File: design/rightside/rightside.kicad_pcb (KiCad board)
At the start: 4 copper layers, 142.6 x 96.2 mm, 227 parts, among them IC2 XC9148G50CER-G, IC3 nRF52833-QDAA-R7, IC4 74AHCT125PW,118, IC5 MCP23018T-E_SS, IC6 XC9291B33D1R-G, J1 USB_C_Receptacle_USB2.0_16P, J2 Battery Pos, J3 Battery Neg, J4 OLED_128x32, J6 Conn_01x04, J7 F32Q-1A7H1-11012, U1 BQ27441-G1, U2 BQ24072RGT, U3 USB6B1, U5 PEC11L-4015F-S0015, U6 PEC11L-4015F-S0015, Y1 ECS-320-8-37B2-JTY-TR

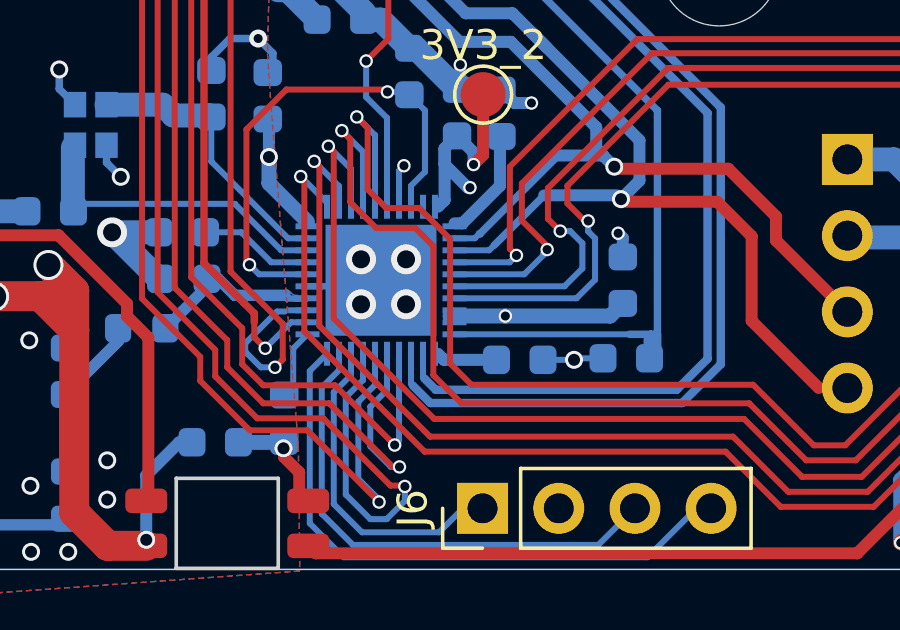
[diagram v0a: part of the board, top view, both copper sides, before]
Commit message: begin routing leftside
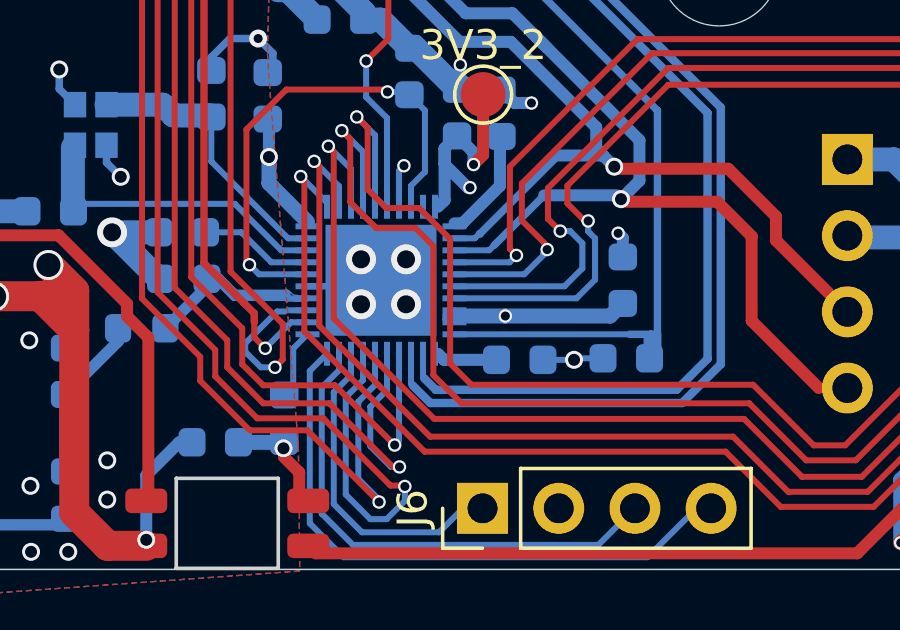
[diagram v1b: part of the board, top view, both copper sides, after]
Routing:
- net 3V3: track 84.2 -> 85.0 mm
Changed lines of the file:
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@@
+	)
+	(segment
+		(start 263.835969 166.079719)
+		(end 263.822288 166.0934)
+		(width 0.2)
+		(layer "B.Cu")
+		(net 2)
 	)
 	(segment
@@
 	)
 	(segment
+		(start 263.822288 166.0934)
+		(end 263.5505 166.0934)
+		(width 0.2)
+		(layer "B.Cu")
+		(net 2)
+	)
+	(segment
 		(start 253.410969 129.355719)
 		(end 251.885969 129.355719)
@@
 	)
 	(segment
+		(start 263.5505 166.0934)
+		(end 263.535969 166.078869)
+		(width 0.2)
+		(layer "B.Cu")
+		(net 2)
+	)
+	(segment
 		(start 276.990969 163.350719)
 		(end 276.930969 163.290719)
@@
 	)
 	(segment
+		(start 263.535969 166.078869)
+		(end 263.535969 165.8934)
+		(width 0.2)
+		(layer "B.Cu")
+		(net 2)
+	)
+	(segment
 		(start 263.505969 160.380719)
 		(end 263.505969 162.109719)
@@
 		(layer "B.Cu")
 		(net 2)
+	)
+	(segment
+		(start 263.835969 165.779719)
+		(end 263.835969 166.079719)
+		(width 0.2)
+		(layer "B.Cu")
+		(net 2)

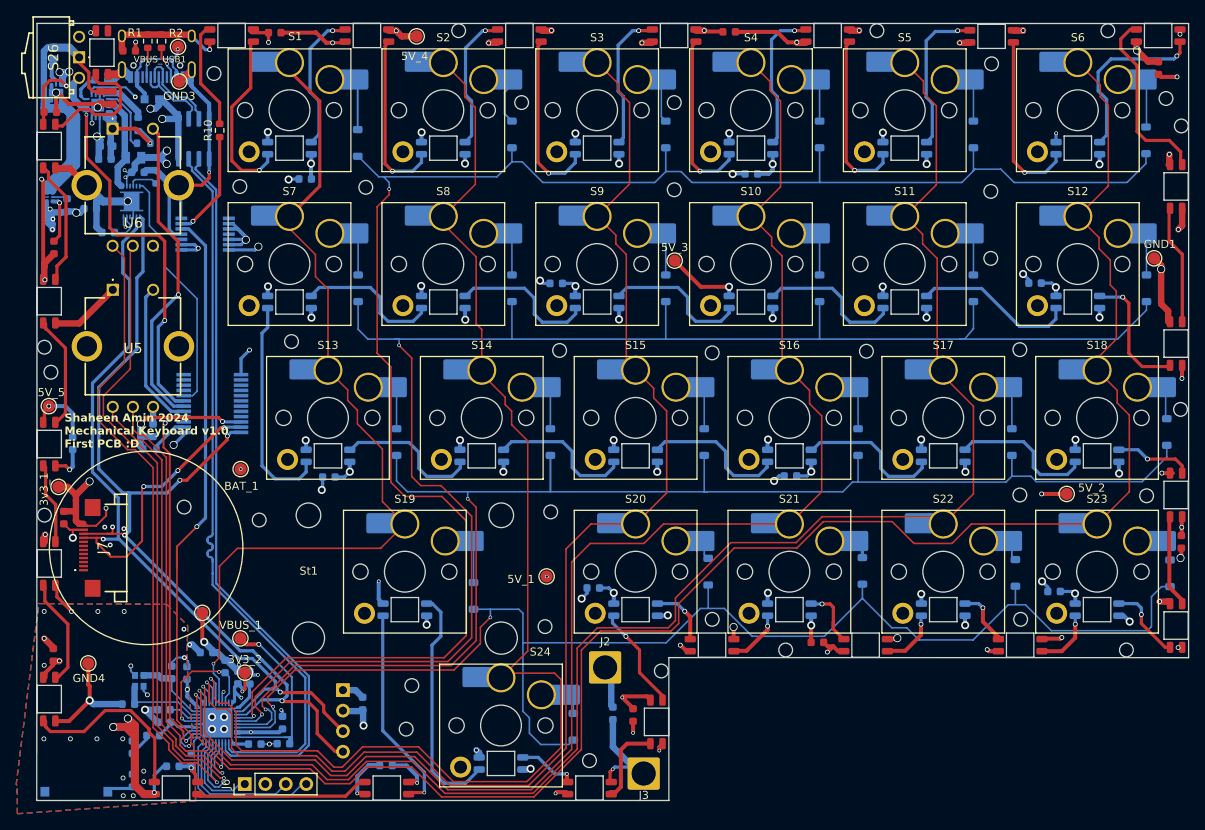
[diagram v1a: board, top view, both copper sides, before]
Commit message: LS routing complete
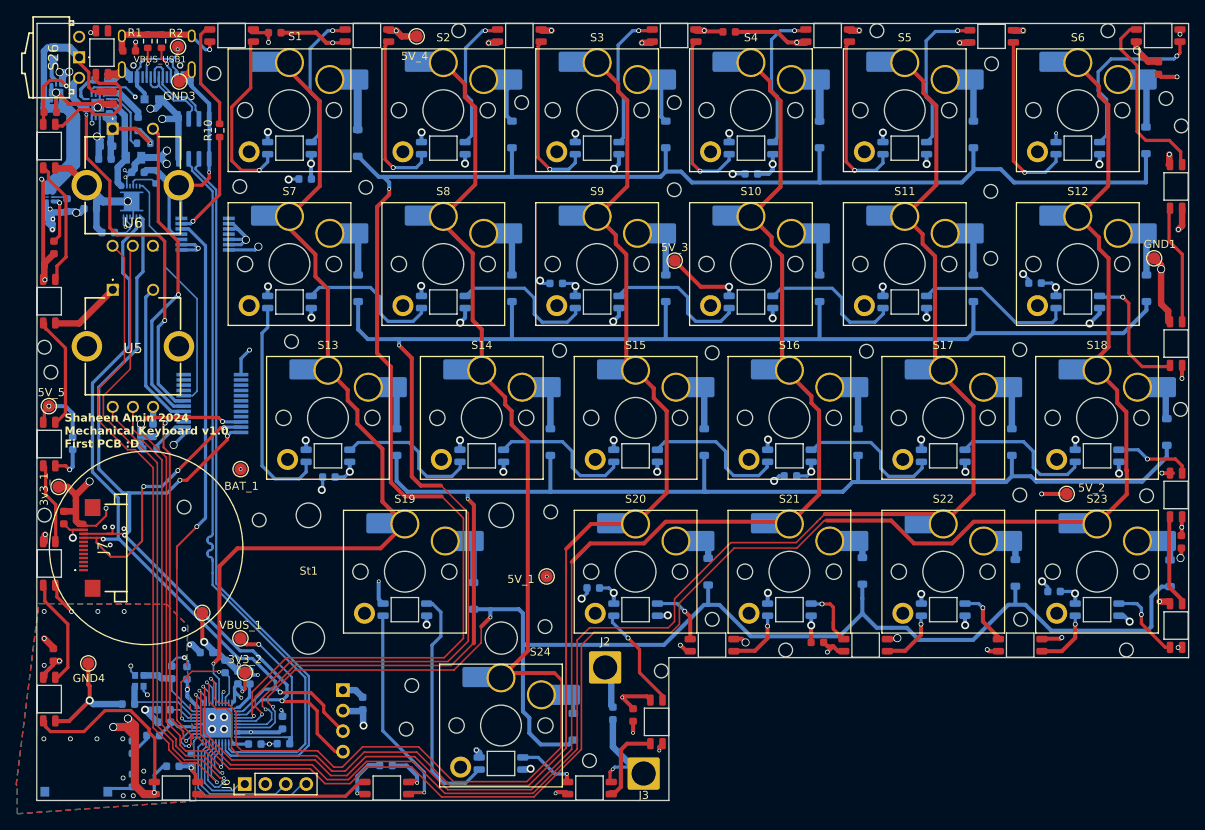
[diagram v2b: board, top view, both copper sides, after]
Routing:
- net GND: track 340.9 -> 343.5 mm
- net /Column 4: track 193.2 -> 195.5 mm
- net /Row 1: track 202.2 -> 200.1 mm
- net 5V: track 167.3 -> 168.2 mm
- net /Row 0: track 216.6 -> 217.5 mm
- net Net-(D5-DOUT): track 21.8 -> 21.0 mm
- net Net-(D3-DOUT): track 21.5 -> 20.8 mm
- net Net-(D34-DOUT): track 7.10 -> 7.71 mm

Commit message: LS RS no error
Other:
- board text added: "Shaheen. A 2024 Mechanical Keyboard v1.0 First PCB :D"
- board text removed: "Shaheen Amin 2024 Mechanical Keyboard v1.0 First PCB :D"
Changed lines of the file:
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@@
 		(layer "Edge.Cuts")
 	)
-	(gr_text "Shaheen Amin 2024\nMechanical Keyboard v1.0\nFirst PCB :D"
-		(at 242.440969 130.830719 0)
+	(gr_text "Shaheen. A 2024\nMechanical Keyboard\nv1.0\nFirst PCB :D"
+		(at 250.6005 145.653652 0)
 		(layer "F.SilkS")
 		(effects
 			(font
-				(size 1 1)
-				(thickness 0.25)
+				(size 0.8 0.8)
+				(thickness 0.2)
 				(bold yes)
 			)
@@
 		(polygon
 			(pts
-				(xy 248.218225 172.09476) (xy 248.228225 173.19476) (xy 251.758225 173.23476) (xy 251.788225 170.28476)
-				(xy 251.670969 167.920719) (xy 251.720969 167.180719) (xy 255.100969 167.170719) (xy 257.070969 166.960719)
-				(xy 258.878225 165.60476) (xy 258.678225 164.93476) (xy 255.310969 164.200719) (xy 251.970969 163.870719)
-				(xy 251.530969 165.450719) (xy 250.000969 166.110719) (xy 250.098225 168.29476) (xy 250.260969 171.980719)
+				(xy 248.221636 172.469948) (xy 248.228225 173.19476) (xy 251.758225 173.23476) (xy 251.788225 170.28476)
+				(xy 251.901793 168.151543) (xy 252.8505 167.180719) (xy 254.3505 167.170719) (xy 255.725781 165.615531)
+				(xy 258.878225 165.60476) (xy 258.678225 164.93476) (xy 255.1505 164.336783) (xy 254.480437 165.545781)
+				(xy 252.0005 165.746349) (xy 251.845029 166.583418) (xy 250.098225 168.29476) (xy 250.277503 172.355175)
 			)
 		)

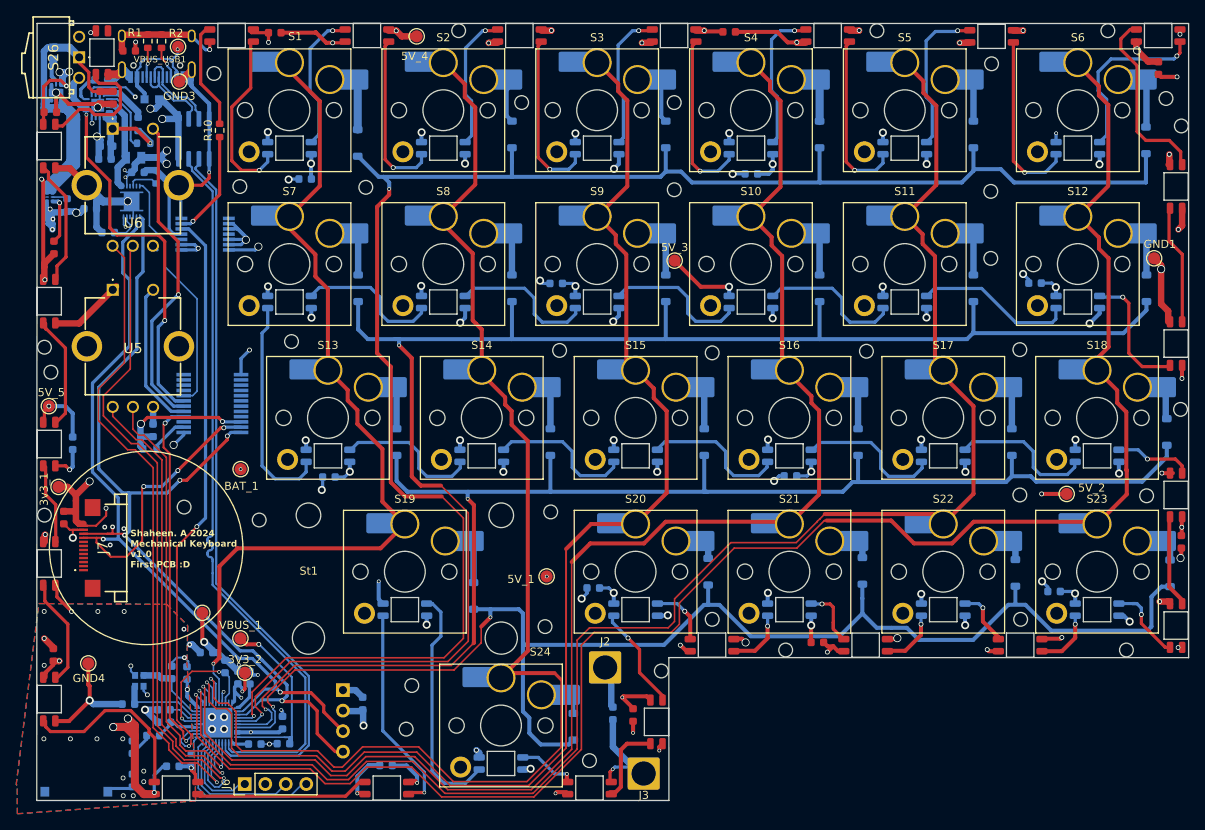
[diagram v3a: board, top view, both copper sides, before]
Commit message: expand power planes
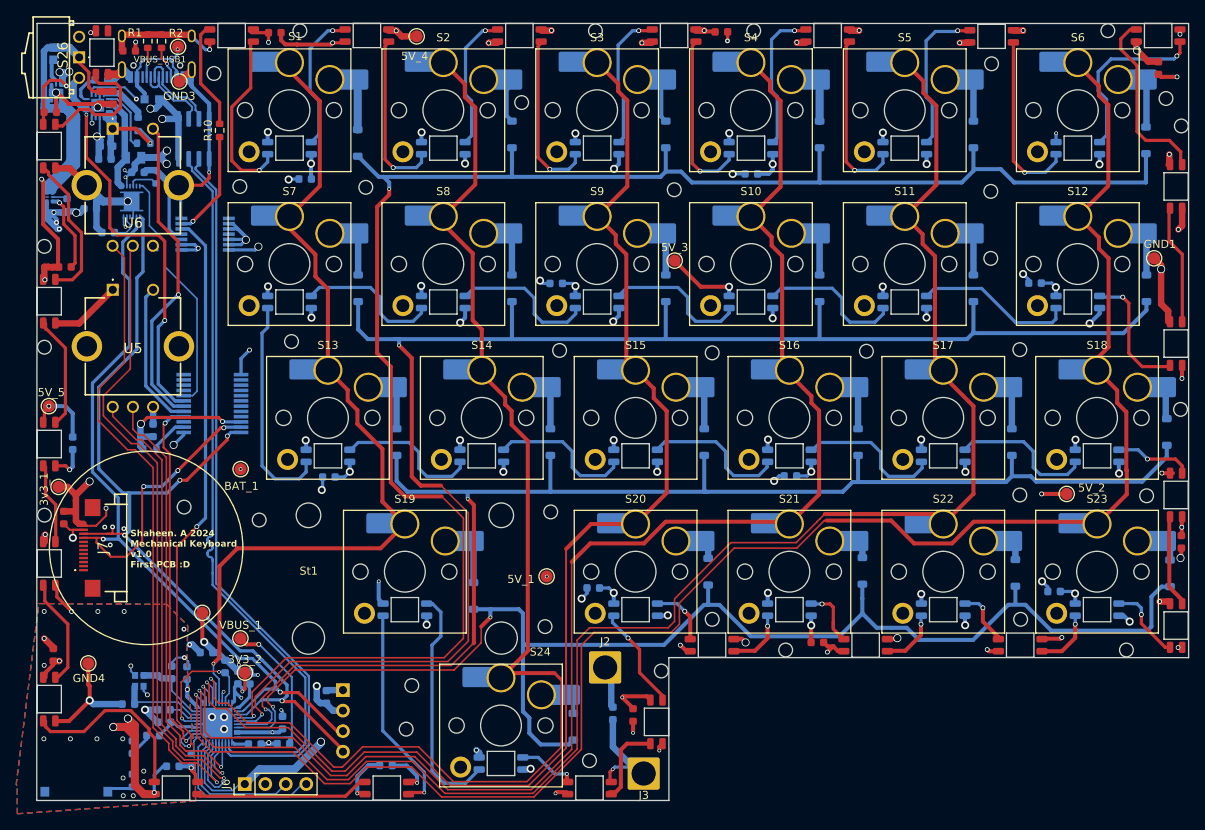
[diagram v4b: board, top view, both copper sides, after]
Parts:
- removed the REF** at (291.3, 79.1)
- removed the REF** at (240.8, 121.4)
- removed the REF** at (343.1, 79.1)
- added REF**: M1.6 Hole, CustomLibrary:M1.6 Hole, F.Cu at (240.0, 105.8)
- added REF**: M1.6 Hole, CustomLibrary:M1.6 Hole, F.Cu at (327.8, 79.1)
- added REF**: M1.6 Hole, CustomLibrary:M1.6 Hole, F.Cu at (271.6, 79.1)
- moved REF** 13.2 mm to (308.2, 79.1)
- moved C9 4.56 mm to (274.9, 161.6)
- moved C46 2.77 mm to (242.5, 108.3), turned to 180 degrees
- moved C41 0.96 mm to (323.8, 79.2)
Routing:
- net 3V3: track 85.0 -> 98.7 mm, vias 14 -> 15
- net GND: track 343.5 -> 340.5 mm
- net Net-(D46-DOUT): track 15.4 -> 18.1 mm
- net /Column 2: track 160.2 -> 157.7 mm
- net /Column 1: track 161.0 -> 158.5 mm
- net 5V: track 168.2 -> 169.9 mm
- net /SDA: track 117.0 -> 115.5 mm
